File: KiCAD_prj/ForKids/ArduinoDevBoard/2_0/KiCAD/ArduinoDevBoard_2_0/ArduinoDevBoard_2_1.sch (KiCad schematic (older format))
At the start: 44 parts, among them J1 Conn_01x04_Female, J10 Conn_01x04_Female, J11 Conn_01x04_Female, J12 Conn_01x02_Female, J13 Conn_01x15_Female, J14 Conn_01x15_Female, J2 Conn_01x04_Female, J3 Conn_01x05_Female, J4 Screw_Terminal_01x02, J5 Conn_01x02_Female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

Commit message: Update ArduinoDevBoard 2.1 pcb
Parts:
- J13, J14: footprint (none) -> Connector_PinHeader_2.54mm:PinHeader_1x15_P2.54mm_Vertical
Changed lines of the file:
@@
 F 0 "J13" H 3842 4243 50  0000 C CNN
 F 1 "Conn_01x15_Female" H 3842 4244 50  0001 C CNN
-F 2 "" H 3950 3450 50  0001 C CNN
+F 2 "Connector_PinHeader_2.54mm:PinHeader_1x15_P2.54mm_Vertical" H 3950 3450 50  0001 C CNN
 F 3 "~" H 3950 3450 50  0001 C CNN
 	1    3950 3450
@@
 F 0 "J14" H 7342 4293 50  0000 C CNN
 F 1 "Conn_01x15_Female" H 7342 4294 50  0001 C CNN
-F 2 "" H 7450 3500 50  0001 C CNN
+F 2 "Connector_PinHeader_2.54mm:PinHeader_1x15_P2.54mm_Vertical" H 7450 3500 50  0001 C CNN
 F 3 "~" H 7450 3500 50  0001 C CNN
 	1    7450 3500
@@
 	6600 3250 6500 3250
 $Comp
-L power:PWR_FLAG #FLG?
+L power:PWR_FLAG #FLG0104
 U 1 1 5E39482E
 P 5750 2400
-F 0 "#FLG?" H 5750 2475 50  0001 C CNN
+F 0 "#FLG0104" H 5750 2475 50  0001 C CNN
 F 1 "PWR_FLAG" H 5750 2573 50  0001 C CNN
 F 2 "" H 5750 2400 50  0001 C CNN

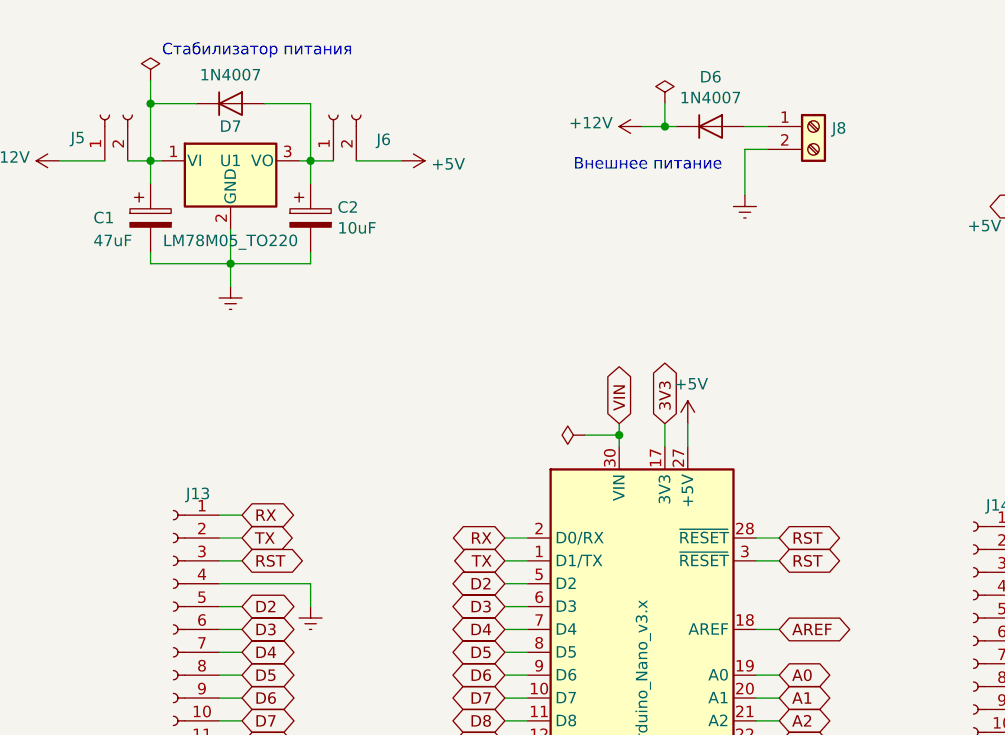
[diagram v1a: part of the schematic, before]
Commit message: Update  ArduinoDevBoard 2.1 project
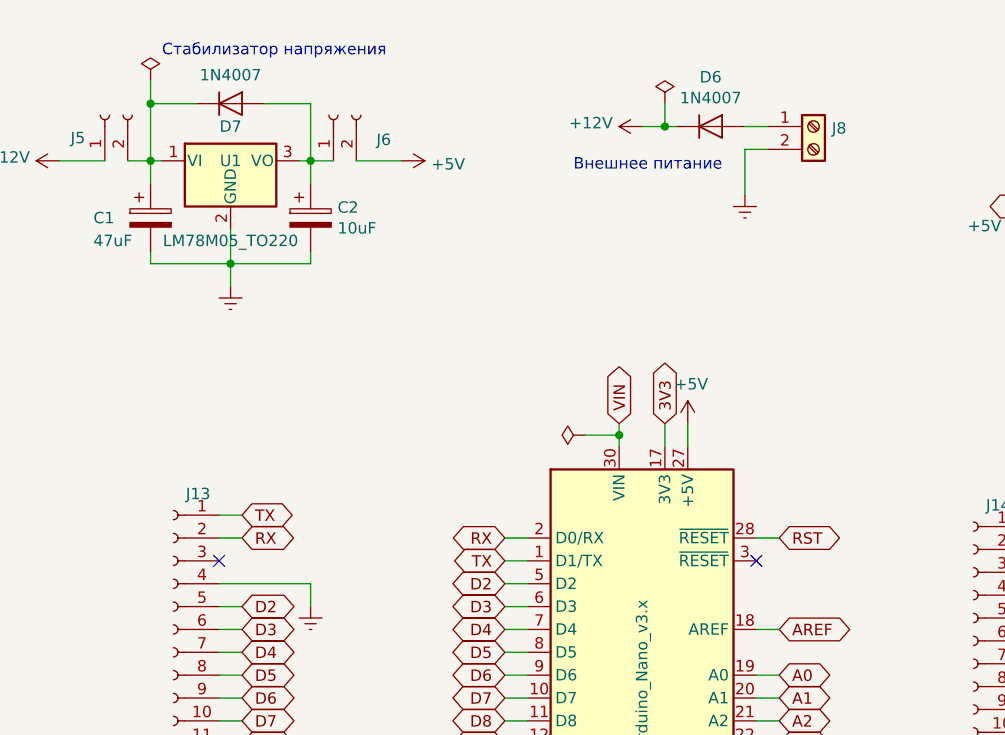
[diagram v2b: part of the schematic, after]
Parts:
- J13, J14: footprint Connector_PinHeader_2.54mm:PinHeader_1x15_P2.54mm_Vertical -> Connector_PinSocket_2.54mm:PinSocket_1x15_P2.54mm_Vertical
- J2: footprint Connector_PinHeader_2.54mm:PinHeader_1x04_P2.54mm_Vertical -> Connector_PinSocket_2.54mm:PinSocket_1x04_P2.54mm_Vertical
- J9: footprint Connector_PinHeader_2.54mm:PinHeader_1x03_P2.54mm_Vertical -> Connector_PinSocket_2.54mm:PinSocket_1x03_P2.54mm_Vertical
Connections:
- net RST: no longer A1.3 (~RESET), J13.3 (Pin_3)
- net RX: now also J13.2 (Pin_2); no longer J13.1 (Pin_1)
- net TX: now also J13.1 (Pin_1); no longer J13.2 (Pin_2)
- no-connect marks 0 -> 2
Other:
- note added: "Стабилизатор напряжения"
- note removed: "Стабилизатор питания"
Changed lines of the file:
@@
 F 0 "J2" H 2428 3776 50  0000 L CNN
 F 1 "Conn_01x04_Female" H 2428 3685 50  0001 L CNN
-F 2 "Connector_PinHeader_2.54mm:PinHeader_1x04_P2.54mm_Vertical" H 2400 3800 50  0001 C CNN
+F 2 "Connector_PinSocket_2.54mm:PinSocket_1x04_P2.54mm_Vertical" H 2400 3800 50  0001 C CNN
 F 3 "~" H 2400 3800 50  0001 C CNN
 	1    2400 3800
@@
 F 0 "J9" H 8228 1426 50  0000 L CNN
 F 1 "Conn_01x03_Female" H 8228 1335 50  0001 L CNN
-F 2 "Connector_PinHeader_2.54mm:PinHeader_1x03_P2.54mm_Vertical" H 8200 1400 50  0001 C CNN
+F 2 "Connector_PinSocket_2.54mm:PinSocket_1x03_P2.54mm_Vertical" H 8200 1400 50  0001 C CNN
 F 3 "~" H 8200 1400 50  0001 C CNN
 	1    8200 1400
@@
 Мотор
 Text Notes 3900 750  0    50   ~ 0
-Стабилизатор питания
+Стабилизатор напряжения
 Text Notes 7800 1150 0    50   ~ 0
 Датчик t\nDS18B20
@@
 F 0 "J13" H 3842 4243 50  0000 C CNN
 F 1 "Conn_01x15_Female" H 3842 4244 50  0001 C CNN
-F 2 "Connector_PinHeader_2.54mm:PinHeader_1x15_P2.54mm_Vertical" H 3950 3450 50  0001 C CNN
+F 2 "Connector_PinSocket_2.54mm:PinSocket_1x15_P2.54mm_Vertical" H 3950 3450 50  0001 C CNN
 F 3 "~" H 3950 3450 50  0001 C CNN
 	1    3950 3450
@@
 Wire Wire Line
 	5400 2950 5500 2950
+Text GLabel 4250 2850 2    50   BiDi ~ 0
+RX
+Wire Wire Line
+	4250 2750 4150 2750
 Text GLabel 4250 2750 2    50   BiDi ~ 0
-RX
-Wire Wire Line
-	4250 2750 4150 2750
-Text GLabel 4250 2850 2    50   BiDi ~ 0
 TX
 Wire Wire Line
@@
 Text GLabel 4250 3150 2    50   BiDi ~ 0
 D2
-Wire Wire Line
-	4250 2950 4150 2950
 Text GLabel 4250 3250 2    50   BiDi ~ 0
 D3
@@
 Wire Wire Line
 	4150 3050 4550 3050
-Text GLabel 6600 2950 2    50   BiDi ~ 0
-RST
-Wire Wire Line
-	6600 2950 6500 2950
 Text GLabel 6600 2850 2    50   BiDi ~ 0
-RST
-Wire Wire Line
-	6600 2850 6500 2850
-Text GLabel 4250 2950 2    50   BiDi ~ 0
 RST
 $Comp
@@
 F 0 "J14" H 7342 4293 50  0000 C CNN
 F 1 "Conn_01x15_Female" H 7342 4294 50  0001 C CNN
-F 2 "Connector_PinHeader_2.54mm:PinHeader_1x15_P2.54mm_Vertical" H 7450 3500 50  0001 C CNN
+F 2 "Connector_PinSocket_2.54mm:PinSocket_1x15_P2.54mm_Vertical" H 7450 3500 50  0001 C CNN
 F 3 "~" H 7450 3500 50  0001 C CNN
 	1    7450 3500
@@
 Wire Wire Line
 	5900 2400 5900 2450
+NoConn ~ 4150 2950
+Wire Wire Line
+	6600 2850 6500 2850
+NoConn ~ 6500 2950
 $EndSCHEMATC

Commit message: Update ArduinoDevBoard 2.1 rev  1.0
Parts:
- U1: footprint Package_TO_SOT_THT:TO-220-3_Vertical -> Package_TO_SOT_THT:TO-92_Wide
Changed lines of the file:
@@
 F 0 "U1" H 4200 1200 50  0000 C CNN
 F 1 "LM78M05_TO220" H 4200 850 50  0000 C CNN
-F 2 "Package_TO_SOT_THT:TO-220-3_Vertical" H 4200 1425 50  0001 C CIN
+F 2 "Package_TO_SOT_THT:TO-92_Wide" H 4200 1425 50  0001 C CIN
 F 3 "http://www.fairchildsemi.com/ds/LM/LM78M05.pdf" H 4200 1150 50  0001 C CNN
 	1    4200 1200
